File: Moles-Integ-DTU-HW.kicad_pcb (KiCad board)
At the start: 2 copper layers, 87 x 68 mm, 78 parts, among them J1 PWR, J2 USB_B_Mini, J3 DISP, J4 PROG, J5 RF_MOD, J6 SMA, J7 U.FL, Q1 MMSS8050-H-TP, Q2 MMSS8050-H-TP, SW1 BOOT, SW2 EN, U1 AZ1117-3.3, U2 ESP32-WROOM-32D, U3 nRF24L01P, U4 WE-TVS-824001, U5 CP2102N-Axx-xQFN28, Y1 16MHz

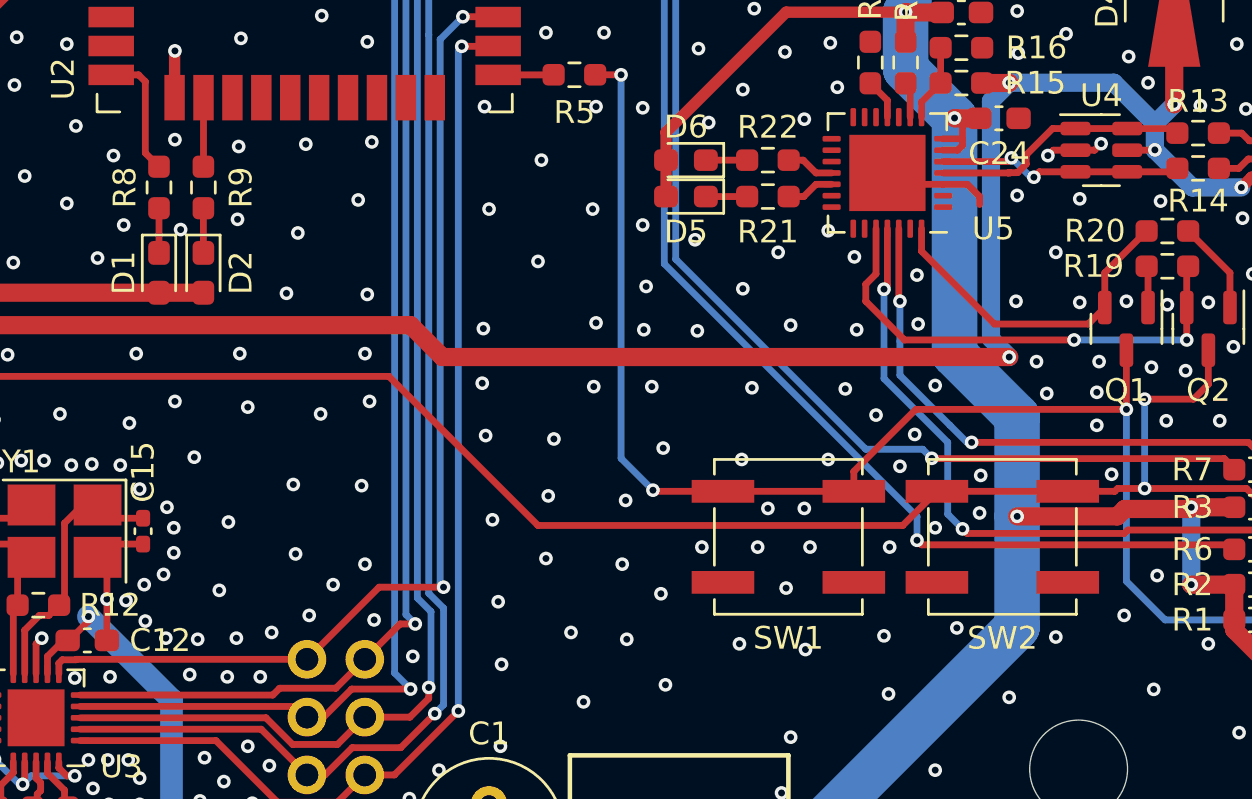
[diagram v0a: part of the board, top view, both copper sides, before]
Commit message: Added Text to PCB silkscreen and updated 3D
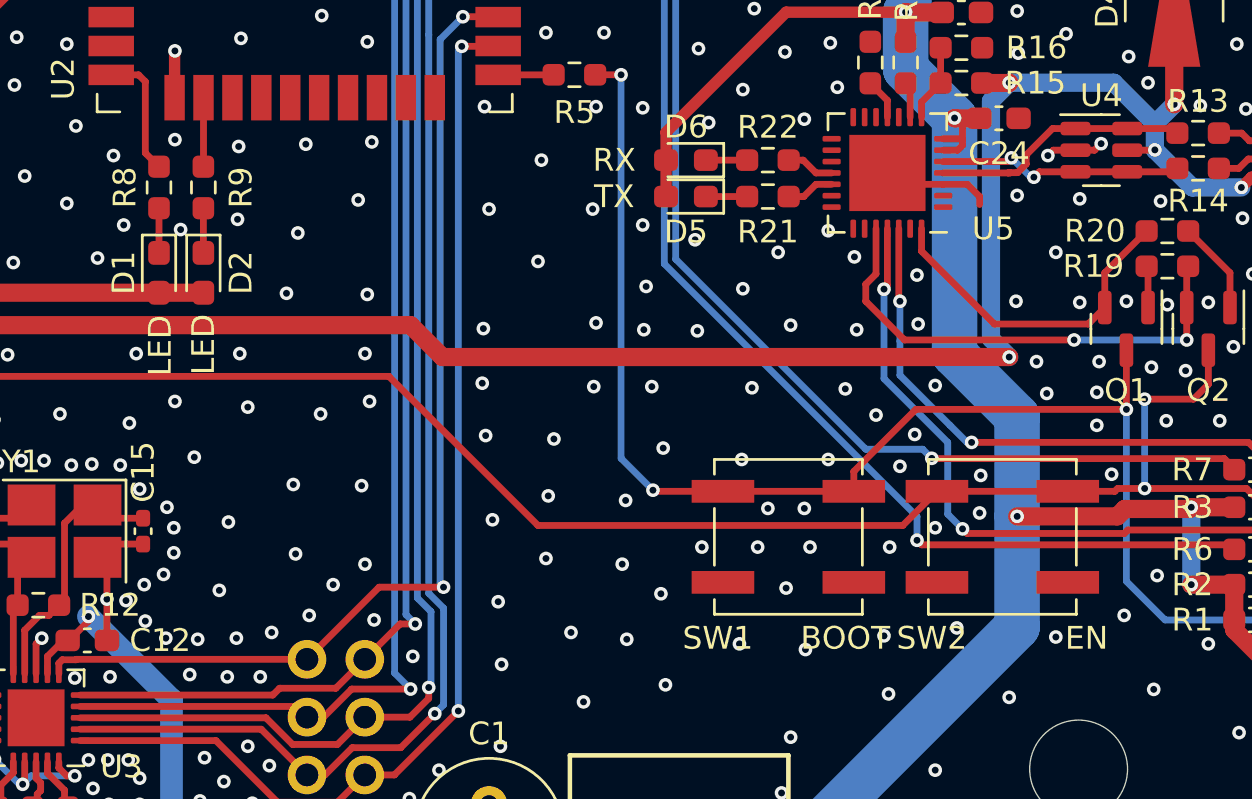
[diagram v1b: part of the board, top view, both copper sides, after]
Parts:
- D5: value LED -> TX
- D6: value LED -> RX
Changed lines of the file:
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@@
   (net 46 "Net-(C9-Pad1)")
   (net 47 "Net-(C11-Pad1)")
-  (net 48 "Net-(R12-Pad1)")
-  (net 49 "Net-(R12-Pad2)")
+  (net 48 "Net-(C14-Pad1)")
+  (net 49 "Net-(C15-Pad1)")
   (net 50 "Net-(C17-Pad1)")
   (net 51 "Net-(C17-Pad2)")
@@
   (net 83 "Net-(D5-Pad1)")
   (net 84 "Net-(D6-Pad1)")
-  (net 85 "Net-(U5-Pad11)")
-  (net 86 "Net-(U5-Pad19)")
-  (net 87 "Net-(U5-Pad18)")
+  (net 85 "Net-(R18-Pad1)")
+  (net 86 "Net-(R21-Pad1)")
+  (net 87 "Net-(R22-Pad1)")
   (footprint "Resistor_SMD:R_0603_1608Metric_Pad0.98x0.95mm_HandSolder" (layer "F.Cu")
     (at 146.7 85.2 180)
@@
     (fp_line (start 0.8 -0.4125) (end 0.8 0.4125) (layer "F.Fab") (width 0.1))
     (pad "1" smd roundrect (at -0.9125 0 180) (size 0.975 0.95) (layers "F.Cu" "F.Paste" "F.Mask") (roundrect_rratio 0.25)
-      (net 86 "Net-(U5-Pad19)") (pintype "passive"))
+      (net 86 "Net-(R21-Pad1)") (pintype "passive"))
     (pad "2" smd roundrect (at 0.9125 0 180) (size 0.975 0.95) (layers "F.Cu" "F.Paste" "F.Mask") (roundrect_rratio 0.25)
       (net 83 "Net-(D5-Pad1)") (pintype "passive"))
@@
     (fp_line (start -0.8 0.4125) (end -0.8 -0.4125) (layer "F.Fab") (width 0.1))
     (pad "1" smd roundrect (at -0.9125 0 90) (size 0.975 0.95) (layers "F.Cu" "F.Paste" "F.Mask") (roundrect_rratio 0.25)
-      (net 85 "Net-(U5-Pad11)") (pintype "passive"))
+      (net 85 "Net-(R18-Pad1)") (pintype "passive"))
     (pad "2" smd roundrect (at 0.9125 0 90) (size 0.975 0.95) (layers "F.Cu" "F.Paste" "F.Mask") (roundrect_rratio 0.25)
       (net 2 "GND") (pintype "passive"))
@@
     (fp_line (start 0.8 -0.4125) (end 0.8 0.4125) (layer "F.Fab") (width 0.1))
     (pad "1" smd roundrect (at -0.9125 0 180) (size 0.975 0.95) (layers "F.Cu" "F.Paste" "F.Mask") (roundrect_rratio 0.25)
-      (net 87 "Net-(U5-Pad18)") (pintype "passive"))
+      (net 87 "Net-(R22-Pad1)") (pintype "passive"))
     (pad "2" smd roundrect (at 0.9125 0 180) (size 0.975 0.95) (layers "F.Cu" "F.Paste" "F.Mask") (roundrect_rratio 0.25)
       (net 84 "Net-(D6-Pad1)") (pintype "passive"))
@@
       (net 70 "unconnected-(U5-Pad10)") (pinfunction "NC") (pintype "no_connect"))
     (pad "11" smd roundrect (at 0 2.45 180) (size 0.25 0.8) (layers "F.Cu" "F.Paste" "F.Mask") (roundrect_rratio 0.25)
-      (net 85 "Net-(U5-Pad11)") (pinfunction "~{SUSPEND}") (pintype "output"))
+      (net 85 "Net-(R18-Pad1)") (pinfunction "~{SUSPEND}") (pintype "output"))
     (pad "12" smd roundrect (at 0.5 2.45 180) (size 0.25 0.8) (layers "F.Cu" "F.Paste" "F.Mask") (roundrect_rratio 0.25)
       (net 71 "unconnected-(U5-Pad12)") (pinfunction "SUSPEND") (pintype "output+no_connect"))
@@
       (net 76 "unconnected-(U5-Pad17)") (pinfunction "RS485/GPIO.2") (pintype "bidirectional+no_connect"))
     (pad "18" smd roundrect (at 2.45 0 180) (size 0.8 0.25) (layers "F.Cu" "F.Paste" "F.Mask") (roundrect_rratio 0.25)
-      (net 87 "Net-(U5-Pad18)") (pinfunction "~{RXT}/GPIO.1") (pintype "bidirectional"))
+      (net 87 "Net-(R22-Pad1)") (pinfunction "~{RXT}/GPIO.1") (pintype "bidirectional"))
     (pad "19" smd roundrect (at 2.45 -0.5 180) (size 0.8 0.25) (layers "F.Cu" "F.Paste" "F.Mask") (roundrect_rratio 0.25)
-      (net 86 "Net-(U5-Pad19)") (pinfunction "~{TXT}/GPIO.0") (pintype "bidirectional"))
+      (net 86 "Net-(R21-Pad1)") (pinfunction "~{TXT}/GPIO.0") (pintype "bidirectional"))
     (pad "20" smd roundrect (at 2.45 -1 180) (size 0.8 0.25) (layers "F.Cu" "F.Paste" "F.Mask") (roundrect_rratio 0.25)
       (net 77 "unconnected-(U5-Pad20)") (pinfunction "GPIO.6") (pintype "bidirectional+no_connect"))
@@
     (property "Sheetname" "")
     (attr smd)
-    (fp_text reference "SW2" (at 0 -4.45) (layer "F.SilkS")
+    (fp_text reference "SW2" (at 3.1 -4.45) (layer "F.SilkS")
       (effects (font (size 1 1) (thickness 0.15)))
     )
-    (fp_text value "EN" (at 0 0) (layer "F.Fab")
+    (fp_text value "EN" (at -3.7 -4.45) (layer "F.SilkS")
       (effects (font (size 1 1) (thickness 0.15)))
     )
@@
     (fp_line (start 0.5 -0.25) (end 0.5 0.25) (layer "F.Fab") (width 0.1))
     (pad "1" smd roundrect (at -0.5675 0 270) (size 0.735 0.62) (layers "F.Cu" "F.Paste" "F.Mask") (roundrect_rratio 0.25)
-      (net 49 "Net-(R12-Pad2)") (pintype "passive"))
+      (net 49 "Net-(C15-Pad1)") (pintype "passive"))
     (pad "2" smd roundrect (at 0.5675 0 270) (size 0.735 0.62) (layers "F.Cu" "F.Paste" "F.Mask") (roundrect_rratio 0.25)
       (net 2 "GND") (pintype "passive"))
@@
       (effects (font (size 1 1) (thickness 0.15)))
     )
-    (fp_text value "LED" (at 0 1.46) (layer "F.Fab")
+    (fp_text value "RX" (at 3.15 0) (layer "F.SilkS")
       (effects (font (size 1 1) (thickness 0.15)))
     )
@@
     (fp_line (start -1.6 0.25) (end -0.6 1.25) (layer "F.Fab") (width 0.1))
     (pad "1" smd rect (at -1.45 1.15 180) (size 2.1 1.8) (layers "F.Cu" "F.Paste" "F.Mask")
-      (net 49 "Net-(R12-Pad2)") (pinfunction "1") (pintype "passive"))
+      (net 49 "Net-(C15-Pad1)") (pinfunction "1") (pintype "passive"))
     (pad "2" smd rect (at 1.45 1.15 180) (size 2.1 1.8) (layers "F.Cu" "F.Paste" "F.Mask")
       (net 2 "GND") (pinfunction "2") (pintype "passive"))
     (pad "3" smd rect (at 1.45 -1.15 180) (size 2.1 1.8) (layers "F.Cu" "F.Paste" "F.Mask")
-      (net 48 "Net-(R12-Pad1)") (pinfunction "3") (pintype "passive"))
+      (net 48 "Net-(C14-Pad1)") (pinfunction "3") (pintype "passive"))
     (pad "4" smd rect (at -1.45 -1.15 180) (size 2.1 1.8) (layers "F.Cu" "F.Paste" "F.Mask")
       (net 2 "GND") (pinfunction "4") (pintype "passive"))
@@
       (effects (font (size 1 1) (thickness 0.15)))
     )
-    (fp_text value "LED" (at 0 -1.55) (layer "F.Fab")
+    (fp_text value "TX" (at 3.15 0) (layer "F.SilkS")
       (effects (font (size 1 1) (thickness 0.15)))
     )
@@
       (effects (font (size 1 1) (thickness 0.15)))
     )
-    (fp_text value "LED" (at 0 -1.65 90) (layer "F.Fab")
+    (fp_text value "LED" (at 3.15 0 90) (layer "F.SilkS")
       (effects (font (size 1 1) (thickness 0.15)))
     )
@@
     (property "Sheetname" "")
     (attr smd)
-    (fp_text reference "SW1" (at 0 -4.45) (layer "F.SilkS")
+    (fp_text reference "SW1" (at 3.1 -4.45) (layer "F.SilkS")
       (effects (font (size 1 1) (thickness 0.15)))
     )
-    (fp_text value "BOOT" (at 0.15 -0.1) (layer "F.Fab")
+    (fp_text value "BOOT" (at -2.5 -4.45) (layer "F.SilkS")
       (effects (font (size 1 1) (thickness 0.15)))
     )
@@
       (net 2 "GND") (pinfunction "VSS") (pintype "power_in"))
     (pad "9" smd roundrect (at 0.5 1.9375 180) (size 0.25 0.825) (layers "F.Cu" "F.Paste" "F.Mask") (roundrect_rratio 0.25)
-      (net 49 "Net-(R12-Pad2)") (pinfunction "XC2") (pintype "passive"))
+      (net 49 "Net-(C15-Pad1)") (pinfunction "XC2") (pintype "passive"))
     (pad "10" smd roundrect (at 1 1.9375 180) (size 0.25 0.825) (layers "F.Cu" "F.Paste" "F.Mask") (roundrect_rratio 0.25)
-      (net 48 "Net-(R12-Pad1)") (pinfunction "XC1") (pintype "passive"))
+      (net 48 "Net-(C14-Pad1)") (pinfunction "XC1") (pintype "passive"))
     (pad "11" smd roundrect (at 1.9375 1 180) (size 0.825 0.25) (layers "F.Cu" "F.Paste" "F.Mask") (roundrect_rratio 0.25)
       (net 47 "Net-(C11-Pad1)") (pinfunction "VDD_PA") (pintype "power_out"))
@@
     (fp_line (start 0.5 0.25) (end -0.5 0.25) (layer "F.Fab") (width 0.1))
     (pad "1" smd roundrect (at -0.5675 0 90) (size 0.735 0.62) (layers "F.Cu" "F.Paste" "F.Mask") (roundrect_rratio 0.25)
-      (net 48 "Net-(R12-Pad1)") (pintype "passive"))
+      (net 48 "Net-(C14-Pad1)") (pintype "passive"))
     (pad "2" smd roundrect (at 0.5675 0 90) (size 0.735 0.62) (layers "F.Cu" "F.Paste" "F.Mask") (roundrect_rratio 0.25)
       (net 2 "GND") (pintype "passive"))
@@
     (fp_line (start 0.8 0.4125) (end -0.8 0.4125) (layer "F.Fab") (width 0.1))
     (pad "1" smd roundrect (at -0.9125 0) (size 0.975 0.95) (layers "F.Cu" "F.Paste" "F.Mask") (roundrect_rratio 0.25)
-      (net 48 "Net-(R12-Pad1)") (pintype "passive"))
+      (net 48 "Net-(C14-Pad1)") (pintype "passive"))
     (pad "2" smd roundrect (at 0.9125 0) (size 0.975 0.95) (layers "F.Cu" "F.Paste" "F.Mask") (roundrect_rratio 0.25)
-      (net 49 "Net-(R12-Pad2)") (pintype "passive"))
+      (net 49 "Net-(C15-Pad1)") (pintype "passive"))
     (model "${KICAD6_3DMODEL_DIR}/Resistor_SMD.3dshapes/R_0603_1608Metric.wrl"
       (offset (xyz 0 0 0))
@@
       (effects (font (size 1 1) (thickness 0.15)))
     )
-    (fp_text value "LED" (at 0 1.55 90) (layer "F.Fab")
+    (fp_text value "LED" (at 3.2 -0.05 90) (layer "F.SilkS")
       (effects (font (size 1 1) (thickness 0.15)))
     )
